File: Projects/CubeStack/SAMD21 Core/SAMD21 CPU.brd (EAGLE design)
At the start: 63.5 x 76.2 mm, 38 parts, among them Q1 MBT3904DW2T1, Q2 SI2347DS, Q3 SI2347DS, U1 ATSAMD21G-A, U2 SST26VF064B, U3 AZ1117C, X1A PINHD-1X10, X1B PINHD-1X10, X1C PINHD-1X10, X1D PINHD-1X10, X2 10PIN_CORTEX_DEBUGTHRU_HOLE, Y1 FC1610AN

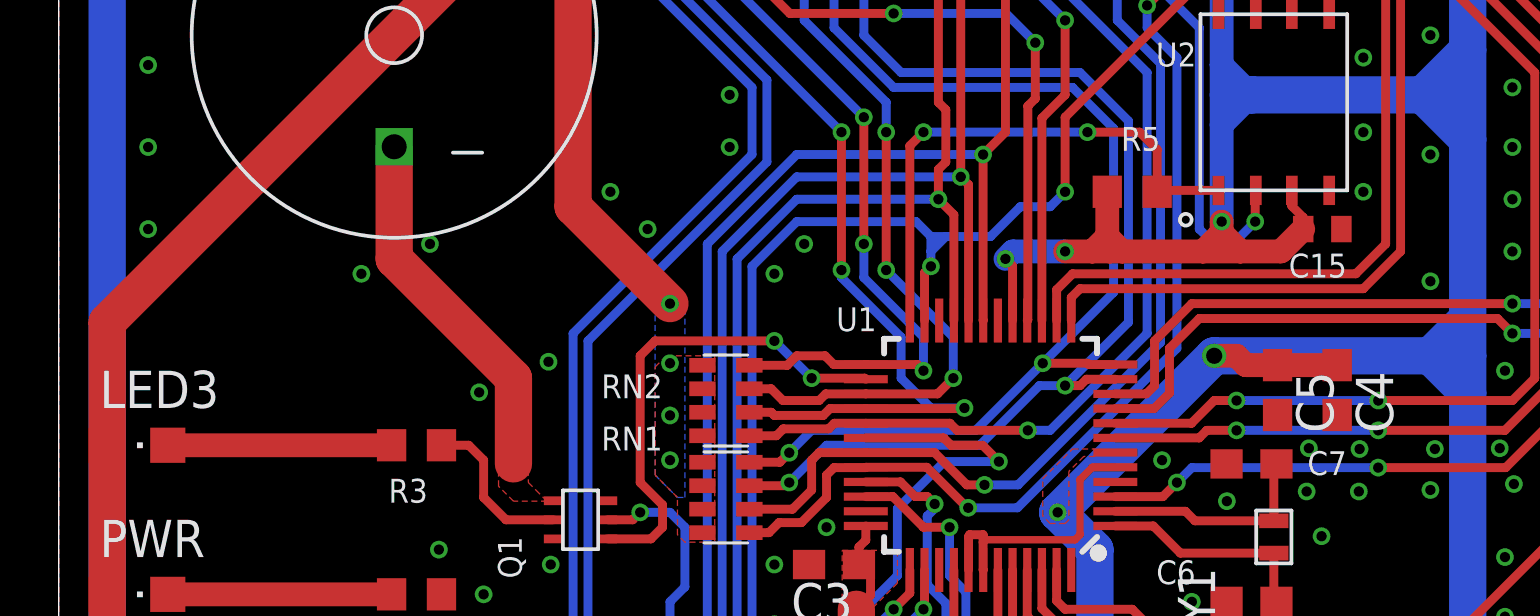
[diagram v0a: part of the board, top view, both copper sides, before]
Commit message: Changed C9 package
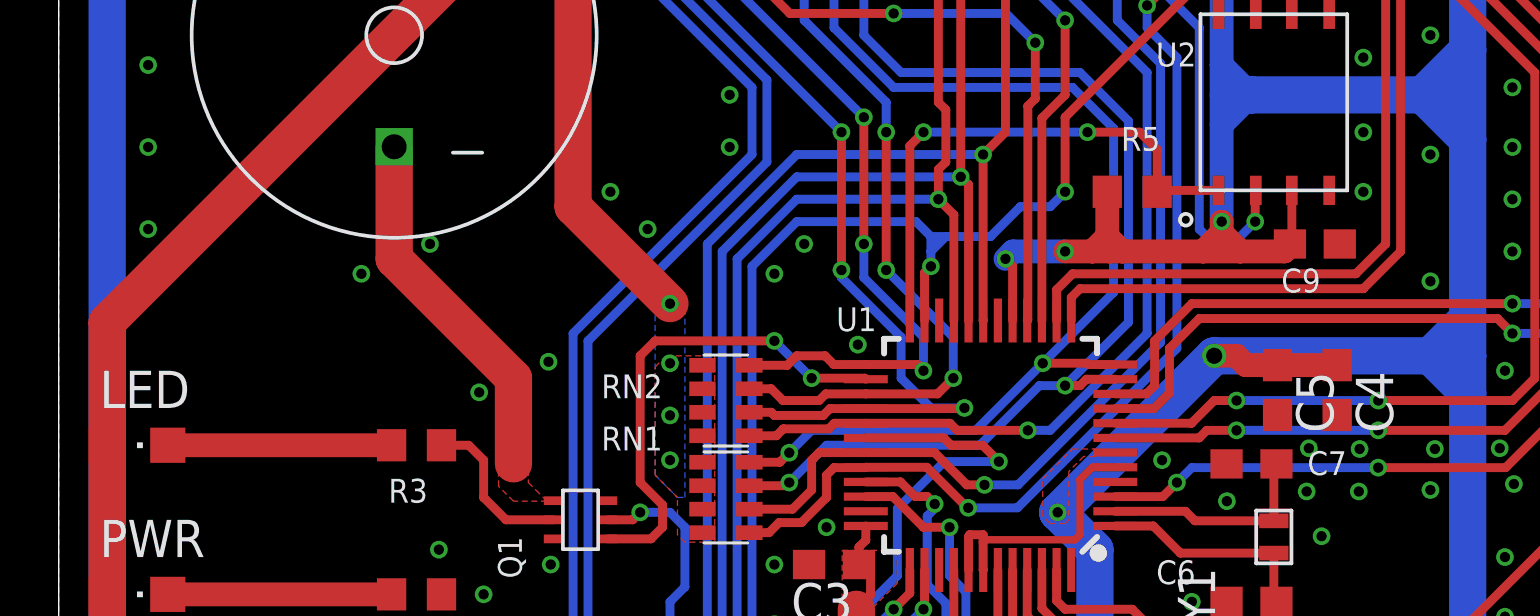
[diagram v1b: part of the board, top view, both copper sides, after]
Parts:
- removed C15: 100n, resistor:C0402
- added C9: 100n, resistor:C0603
- renumbered LED3 to LED
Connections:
- net 3.3V: now also C9.1; no longer C15.1
- net GND: now also C9.2; no longer C15.2
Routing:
- net GND: vias 157 -> 158
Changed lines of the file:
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@@
 <text x="53.34" y="19.812" size="1.27" layer="25">RESET</text>
 <text x="47.752" y="15.748" size="0.8128" layer="25">EN</text>
+<wire x1="43.0022" y1="43.434" x2="43.0022" y2="43.18" width="0.3048" layer="41"/>
+<wire x1="42.926" y1="44.45" x2="42.926" y2="44.196" width="0.3048" layer="41"/>
 </plain>
 <attributes>
@@
 <element name="SJ2" library="CPSS_CONNECTOR" package="SOLBRDG" value="SOLBRDG" x="48.26" y="17.78" smashed="yes" rot="R90"/>
 <element name="RESET" library="CPSS_MISC" package="B3U-1000P" value="1000P" x="50.8" y="20.32" smashed="yes" rot="R90"/>
-<element name="LED3" library="led" library_urn="urn:adsk.eagle:library:259" package="CHIPLED_0805" package3d_urn="urn:adsk.eagle:package:15821/2" value="" x="2.667" y="35.56" smashed="yes" rot="R270">
+<element name="LED" library="led" library_urn="urn:adsk.eagle:library:259" package="CHIPLED_0805" package3d_urn="urn:adsk.eagle:package:15821/2" value="" x="2.667" y="35.56" smashed="yes" rot="R270">
 <attribute name="NAME" x="1.397" y="36.83" size="1.27" layer="25"/>
 <attribute name="VALUE" x="1.397" y="33.02" size="1.27" layer="27"/>
@@
 <attribute name="NAME" x="37.386" y="48.466" size="0.8128" layer="25"/>
 </element>
-<element name="C15" library="resistor" library_urn="urn:adsk.eagle:library:348" package="C0402" package3d_urn="urn:adsk.eagle:package:23626/1" value="100n" x="43.053" y="42.926" smashed="yes">
-<attribute name="NAME" x="41.91" y="41.275" size="0.8128" layer="25"/>
+<element name="C9" library="resistor" library_urn="urn:adsk.eagle:library:348" package="C0603" package3d_urn="urn:adsk.eagle:package:23616/2" value="100n" x="42.799" y="42.418" smashed="yes">
+<attribute name="NAME" x="41.656" y="40.767" size="0.8128" layer="25"/>
 </element>
 <element name="R4" library="rcl" library_urn="urn:adsk.eagle:library:334" package="R0603" package3d_urn="urn:adsk.eagle:package:23555/2" value="1k" x="40.386" y="52.451" smashed="yes">
@@
 <contactref element="RN2" pad="7"/>
 <contactref element="RN2" pad="8"/>
-<contactref element="LED3" pad="A"/>
+<contactref element="LED" pad="A"/>
 <contactref element="PWR" pad="A"/>
 <contactref element="SD" pad="4"/>
 <contactref element="U2" pad="P$8"/>
-<contactref element="C15" pad="1"/>
+<contactref element="C9" pad="1"/>
 <contactref element="U2" pad="P$3"/>
 <contactref element="R4" pad="1"/>
@@
 <wire x1="39.624" y1="51.308" x2="39.624" y2="52.363" width="0.8128" layer="1"/>
 <wire x1="39.624" y1="52.363" x2="39.536" y2="52.451" width="0.8128" layer="1"/>
-<wire x1="42.403" y1="42.926" x2="41.641" y2="42.164" width="0.8128" layer="1"/>
-<wire x1="41.641" y1="42.164" x2="40.259" y2="42.164" width="0.8128" layer="1"/>
+<wire x1="42.0155" y1="42.508165625" x2="41.761665625" y2="42.164" width="0.8128" layer="1"/>
+<wire x1="41.761665625" y1="42.164" x2="40.259" y2="42.164" width="0.8128" layer="1"/>
 <wire x1="40.259" y1="42.164" x2="38.989" y2="42.164" width="0.8128" layer="1"/>
 <wire x1="38.989" y1="42.164" x2="36.234" y2="42.164" width="0.8128" layer="1"/>
@@
 <wire x1="39.624" y1="43.18" x2="39.624" y2="42.799" width="0.8128" layer="1"/>
 <wire x1="39.624" y1="42.799" x2="38.989" y2="42.164" width="0.8128" layer="1"/>
-<wire x1="42.0155" y1="44.244" x2="42.0155" y2="43.7095" width="0.3048" layer="1"/>
-<wire x1="42.403" y1="43.322" x2="42.403" y2="42.926" width="0.3048" layer="1"/>
-<wire x1="42.0155" y1="43.7095" x2="42.403" y2="43.322" width="0.3048" layer="1"/>
+<wire x1="42.0155" y1="44.244" x2="42.0155" y2="42.508165625" width="0.3048" layer="1"/>
 <wire x1="25.4" y1="63.5" x2="22.86" y2="63.5" width="1.27" layer="16"/>
 <wire x1="22.86" y1="63.5" x2="20.32" y2="63.5" width="1.27" layer="16"/>
@@
 <wire x1="40.132" y1="38.608" x2="40.4504" y2="38.2896" width="0.8128" layer="1"/>
 <wire x1="41.529" y1="38.2896" x2="43.561" y2="38.2896" width="0.8128" layer="1"/>
+<wire x1="41.949" y1="42.418" x2="42.0155" y2="42.4845" width="0.3048" layer="1"/>
+<wire x1="42.0155" y1="42.4845" x2="42.0155" y2="42.508165625" width="0.3048" layer="1"/>
 </signal>
 <signal name="GND">
@@
 <contactref element="SD" pad="GND3"/>
 <contactref element="U2" pad="P$4"/>
-<contactref element="C15" pad="2"/>
+<contactref element="C9" pad="2"/>
 <contactref element="C2" pad="2"/>
 <polygon width="0.254" layer="1" rank="2">
@@
 <wire x1="47.625" y1="21.17" x2="48.475" y2="20.32" width="0.3048" layer="1"/>
 <wire x1="48.475" y1="20.32" x2="49.149" y2="20.32" width="0.3048" layer="1"/>
+<via x="27.2288" y="38.989" extent="1-16" drill="0.35"/>
 </signal>
 <signal name="N$1">
@@
 <signal name="L_3">
 <contactref element="R3" pad="2"/>
-<contactref element="LED3" pad="C"/>
+<contactref element="LED" pad="C"/>
 <wire x1="3.717" y1="35.56" x2="11.342" y2="35.56" width="0.8128" layer="1"/>
 </signal>

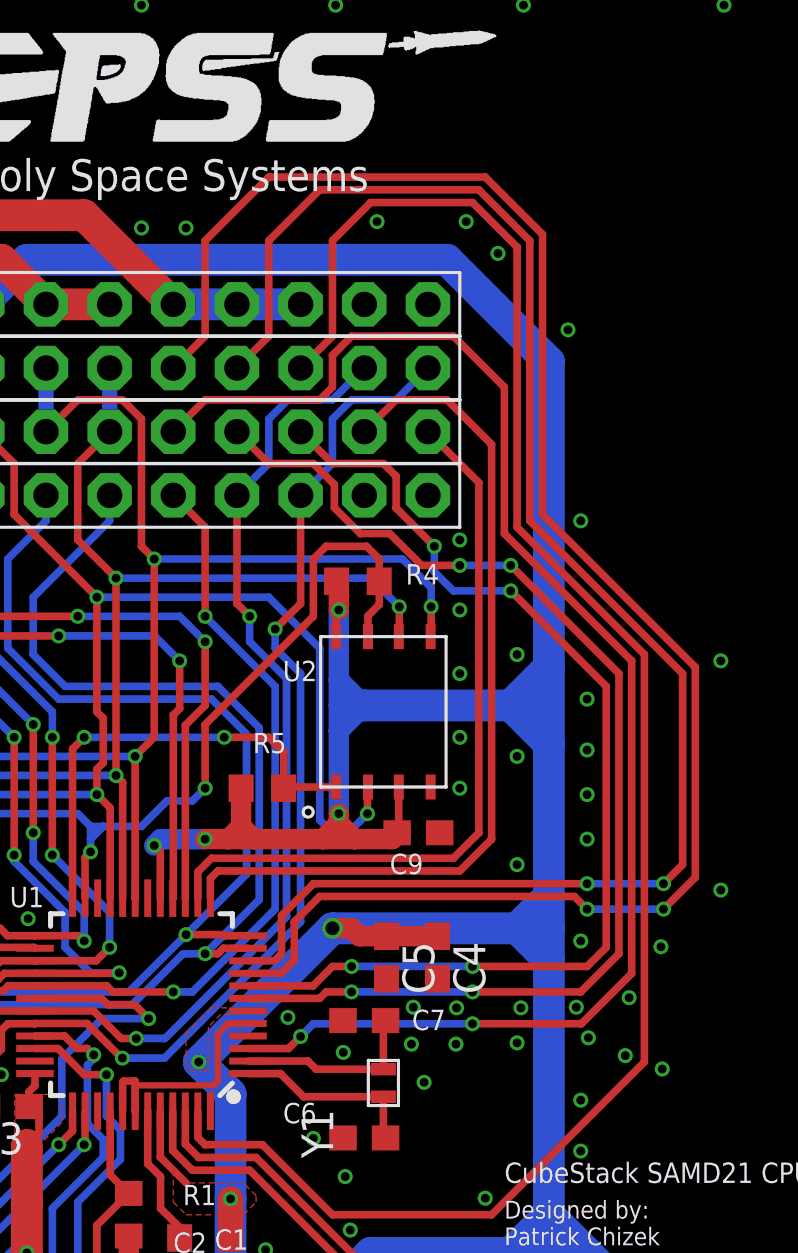
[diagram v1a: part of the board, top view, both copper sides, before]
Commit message: Added more vias to SAMD21 Core
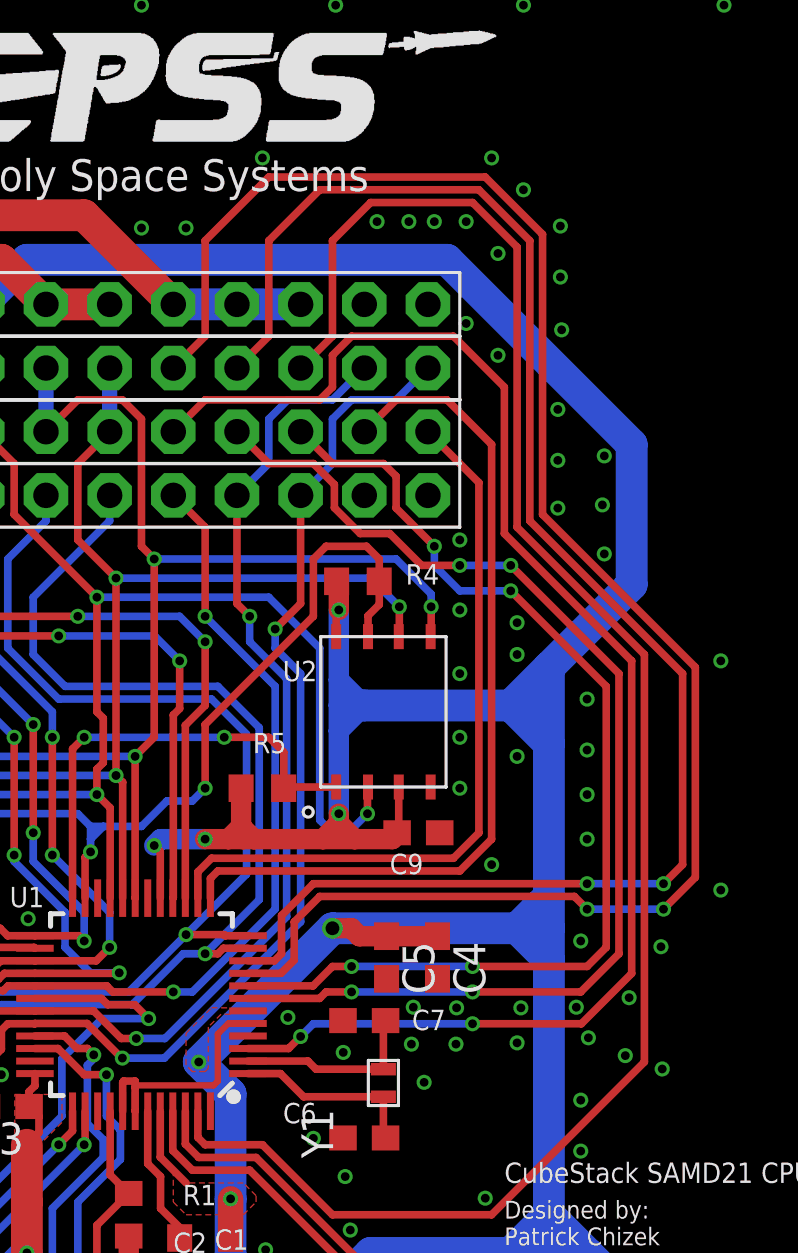
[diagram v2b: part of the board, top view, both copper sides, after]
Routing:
- net 3.3V: track 324.6 -> 327.3 mm
- net GND: vias 158 -> 173
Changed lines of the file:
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@@
 <wire x1="43.0022" y1="43.434" x2="43.0022" y2="43.18" width="0.3048" layer="41"/>
 <wire x1="42.926" y1="44.45" x2="42.926" y2="44.196" width="0.3048" layer="41"/>
+<wire x1="45.212" y1="40.9448" x2="45.212" y2="41.1988" width="0.3048" layer="41"/>
+<wire x1="45.212" y1="40.9448" x2="45.4152" y2="40.7416" width="0.3048" layer="41"/>
+<wire x1="38.608" y1="54.61" x2="38.608" y2="53.848" width="0.3048" layer="42"/>
+<wire x1="37.084" y1="55.372" x2="36.576" y2="55.372" width="0.3048" layer="42"/>
+<wire x1="34.544" y1="55.372" x2="34.036" y2="55.372" width="0.3048" layer="42"/>
+<wire x1="32.004" y1="55.372" x2="31.496" y2="55.372" width="0.3048" layer="42"/>
+<wire x1="29.464" y1="55.372" x2="28.956" y2="55.372" width="0.3048" layer="42"/>
+<wire x1="26.924" y1="55.372" x2="26.416" y2="55.372" width="0.3048" layer="42"/>
+<wire x1="24.384" y1="55.372" x2="23.876" y2="55.372" width="0.3048" layer="42"/>
+<wire x1="21.844" y1="55.372" x2="21.336" y2="55.372" width="0.3048" layer="42"/>
+<wire x1="38.608" y1="62.484" x2="38.608" y2="61.976" width="0.3048" layer="42"/>
+<wire x1="19.812" y1="62.484" x2="19.812" y2="61.976" width="0.3048" layer="42"/>
+<wire x1="39.116" y1="61.468" x2="39.624" y2="61.468" width="0.3048" layer="42"/>
+<wire x1="41.656" y1="61.468" x2="42.164" y2="61.468" width="0.3048" layer="42"/>
+<wire x1="43.688" y1="59.944" x2="43.688" y2="59.436" width="0.3048" layer="42"/>
+<wire x1="41.656" y1="57.912" x2="42.164" y2="57.912" width="0.3048" layer="42"/>
 </plain>
 <attributes>
@@
 </class>
 </classes>
-<designrules name="oshpark-2layer">
+<designrules name="oshpark-2layer *">
 <description language="en">&lt;b&gt;OSH Park Design Rules&lt;/b&gt;
 &lt;p&gt;
@@
 <param name="mlMinCreamFrame" value="0mil"/>
 <param name="mlMaxCreamFrame" value="0mil"/>
-<param name="mlViaStopLimit" value="0mil"/>
+<param name="mlViaStopLimit" value="25mil"/>
 <param name="srRoundness" value="0"/>
 <param name="srMinRoundness" value="0mil"/>
@@
 <wire x1="40.132" y1="47.498" x2="39.624" y2="47.498" width="0.8128" layer="16"/>
 <wire x1="27.178" y1="65.278" x2="43.942" y2="65.278" width="1.27" layer="16"/>
-<wire x1="43.942" y1="65.278" x2="48.006" y2="61.214" width="1.27" layer="16"/>
-<wire x1="48.006" y1="61.214" x2="48.006" y2="49.022" width="1.27" layer="16"/>
+<wire x1="43.942" y1="65.278" x2="51.308" y2="57.912" width="1.27" layer="16"/>
 <wire x1="48.006" y1="49.022" x2="46.482" y2="47.498" width="1.27" layer="16"/>
 <wire x1="46.482" y1="47.498" x2="40.64" y2="47.498" width="1.27" layer="16"/>
@@
 <wire x1="41.949" y1="42.418" x2="42.0155" y2="42.4845" width="0.3048" layer="1"/>
 <wire x1="42.0155" y1="42.4845" x2="42.0155" y2="42.508165625" width="0.3048" layer="1"/>
+<wire x1="51.308" y1="52.324" x2="48.006" y2="49.022" width="1.27" layer="16"/>
+<wire x1="51.308" y1="57.912" x2="51.308" y2="52.324" width="1.27" layer="16"/>
 </signal>
 <signal name="GND">
@@
 <via x="46.736" y="49.53" extent="1-16" drill="0.35"/>
 <via x="46.736" y="45.466" extent="1-16" drill="0.35"/>
-<via x="46.736" y="41.148" extent="1-16" drill="0.35"/>
+<via x="45.72" y="41.148" extent="1-16" drill="0.35"/>
 <via x="49.53" y="42.164" extent="1-16" drill="0.35"/>
 <via x="49.53" y="43.942" extent="1-16" drill="0.35"/>
@@
 <via x="31.242" y="17.526" extent="1-16" drill="0.35"/>
 <via x="52.5272" y="32.9946" extent="1-16" drill="0.35"/>
-<via x="48.768" y="62.484" extent="1-16" drill="0.35"/>
+<via x="48.514" y="62.484" extent="1-16" drill="0.35"/>
 <via x="41.148" y="66.802" extent="1-16" drill="0.35"/>
 <via x="44.704" y="66.802" extent="1-16" drill="0.35"/>
-<via x="45.974" y="65.532" extent="1-16" drill="0.35"/>
+<via x="44.704" y="62.738" extent="1-16" drill="0.35"/>
 <via x="33.528" y="66.548" extent="1-16" drill="0.35"/>
 <via x="31.75" y="66.548" extent="1-16" drill="0.35"/>
@@
 <via x="40.513" y="23.495" extent="1-16" drill="0.35"/>
 <via x="40.0812" y="26.5684" extent="1-16" drill="0.35"/>
-<via x="49.276" y="54.864" extent="1-16" drill="0.35"/>
+<via x="50.2158" y="53.5432" extent="1-16" drill="0.35"/>
 <via x="44.45" y="54.102" extent="1-16" drill="0.35"/>
 <via x="0.762" y="0.762" extent="1-16" drill="0.35"/>
@@
 <wire x1="48.475" y1="20.32" x2="49.149" y2="20.32" width="0.3048" layer="1"/>
 <via x="27.2288" y="38.989" extent="1-16" drill="0.35"/>
+<via x="42.418" y="66.802" extent="1-16" drill="0.35"/>
+<via x="43.434" y="66.802" extent="1-16" drill="0.35"/>
+<via x="45.974" y="61.468" extent="1-16" drill="0.35"/>
+<via x="46.736" y="50.8" extent="1-16" drill="0.35"/>
+<via x="46.99" y="68.072" extent="1-16" drill="0.35"/>
+<via x="45.72" y="69.342" extent="1-16" drill="0.35"/>
+<via x="50.2158" y="57.4548" extent="1-16" drill="0.35"/>
+<via x="48.3616" y="59.309" extent="1-16" drill="0.35"/>
+<via x="48.3616" y="55.372" extent="1-16" drill="0.35"/>
+<via x="45.974" y="65.532" extent="1-16" drill="0.35"/>
+<via x="48.4632" y="64.5922" extent="1-16" drill="0.35"/>
+<via x="48.4632" y="66.6242" extent="1-16" drill="0.35"/>
+<via x="36.576" y="69.342" extent="1-16" drill="0.35"/>
+<via x="48.3616" y="57.277" extent="1-16" drill="0.35"/>
+<via x="50.1396" y="55.499" extent="1-16" drill="0.35"/>
 </signal>
 <signal name="N$1">
@@
 <wire x1="38.2182" y1="31.8858" x2="41.402" y2="31.8858" width="0.3048" layer="1"/>
 <wire x1="38.2182" y1="31.8858" x2="37.294" y2="32.81" width="0.3048" layer="1"/>
-<wire x1="41.402" y1="31.8858" x2="41.49" y2="31.7978" width="0.3048" layer="1"/>
 <wire x1="41.402" y1="31.8858" x2="41.402" y2="30.33" width="0.3048" layer="1"/>
 <wire x1="41.402" y1="30.33" x2="41.49" y2="30.242" width="0.3048" layer="1"/>
@@
 <wire x1="32.258" y1="46.228" x2="32.258" y2="53.34" width="0.3048" layer="1"/>
 <via x="32.258" y="53.34" extent="1-16" drill="0.35"/>
-<wire x1="32.258" y1="53.34" x2="42.164" y2="53.34" width="0.3048" layer="16"/>
-<wire x1="43.307" y1="52.197" x2="43.307" y2="51.435" width="0.3048" layer="16"/>
+<wire x1="32.258" y1="53.34" x2="41.91" y2="53.34" width="0.3048" layer="16"/>
+<wire x1="43.307" y1="51.943" x2="43.307" y2="51.435" width="0.3048" layer="16"/>
 <via x="43.307" y="51.435" extent="1-16" drill="0.35"/>
-<wire x1="42.164" y1="53.34" x2="43.307" y2="52.197" width="0.3048" layer="16"/>
+<wire x1="41.91" y1="53.34" x2="43.307" y2="51.943" width="0.3048" layer="16"/>
 <wire x1="43.307" y1="51.435" x2="43.307" y2="50.264" width="0.3048" layer="1"/>
 <wire x1="43.307" y1="50.264" x2="43.287" y2="50.244" width="0.3048" layer="1"/>
@@
 <wire x1="41.91" y1="55.372" x2="43.434" y2="53.848" width="0.3048" layer="1"/>
 <via x="43.434" y="53.848" extent="1-16" drill="0.35"/>
-<wire x1="43.434" y1="53.848" x2="43.434" y2="52.832" width="0.3048" layer="16"/>
-<wire x1="44.196" y1="52.07" x2="46.482" y2="52.07" width="0.3048" layer="16"/>
+<wire x1="43.434" y1="53.848" x2="43.434" y2="53.086" width="0.3048" layer="16"/>
+<wire x1="44.45" y1="52.07" x2="46.482" y2="52.07" width="0.3048" layer="16"/>
 <via x="46.482" y="52.07" extent="1-16" drill="0.35"/>
-<wire x1="43.434" y1="52.832" x2="44.196" y2="52.07" width="0.3048" layer="16"/>
+<wire x1="43.434" y1="53.086" x2="44.45" y2="52.07" width="0.3048" layer="16"/>
 <wire x1="36" y1="36.31" x2="38.596" y2="36.31" width="0.3048" layer="1"/>
 <wire x1="39.37" y1="37.084" x2="38.596" y2="36.31" width="0.3048" layer="1"/>
@@
 <mfgpreviewcolor name="substratecolor" color="0xFF786E46"/>
 </mfgpreviewcolors>
+<errors>
+</errors>
 </board>
 </drawing>
